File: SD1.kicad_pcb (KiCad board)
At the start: 4 copper layers, 107.8 x 108 mm, 251 parts, among them J101 JST 1.25mm, J102 JST 1.25mm, J103 JST ZH 1.5mm 1x5, J201 HR861153C, J301 PJ-102AH, J302 PJ-102AH, J303 Conn_01x02, J304 Conn_01x02, J402 FTDI_TTL_Cable, J403 10118194-0001LF, J404 Conn_ARM_JTAG_SWD_10, J801 Conn_01x02, J802 Conn_01x02, Q101 BSS138, Q102 PDTC114EU,115, Q301 DMMT5401, Q302 DMMT5401, Q303 FDT86244, Q801 DMMT5401, Q802 DMMT5401, SW101 Multidirection_Switch, SW401 PTS810, T301 HR051067, U101 ER-TFTM028-4, U102 MCP23017, U103 CC2652P, U104 SCD30, U105 BME280, U106 EKMC1691111, U201 W5500, U301 TPS23753A, U302 TL431A, U303 TCMT1107, U401 CP2102N-A02-GQFN28R, U501 CCS811, U601 110-102, U602 LMP91000, U701 TLV70018, U702 ADPD188BI, U703 Smoke Chamber, U801 TPS61022, U802 TLV62585, U803 MCP73831-2-OT, Y201 25MHz

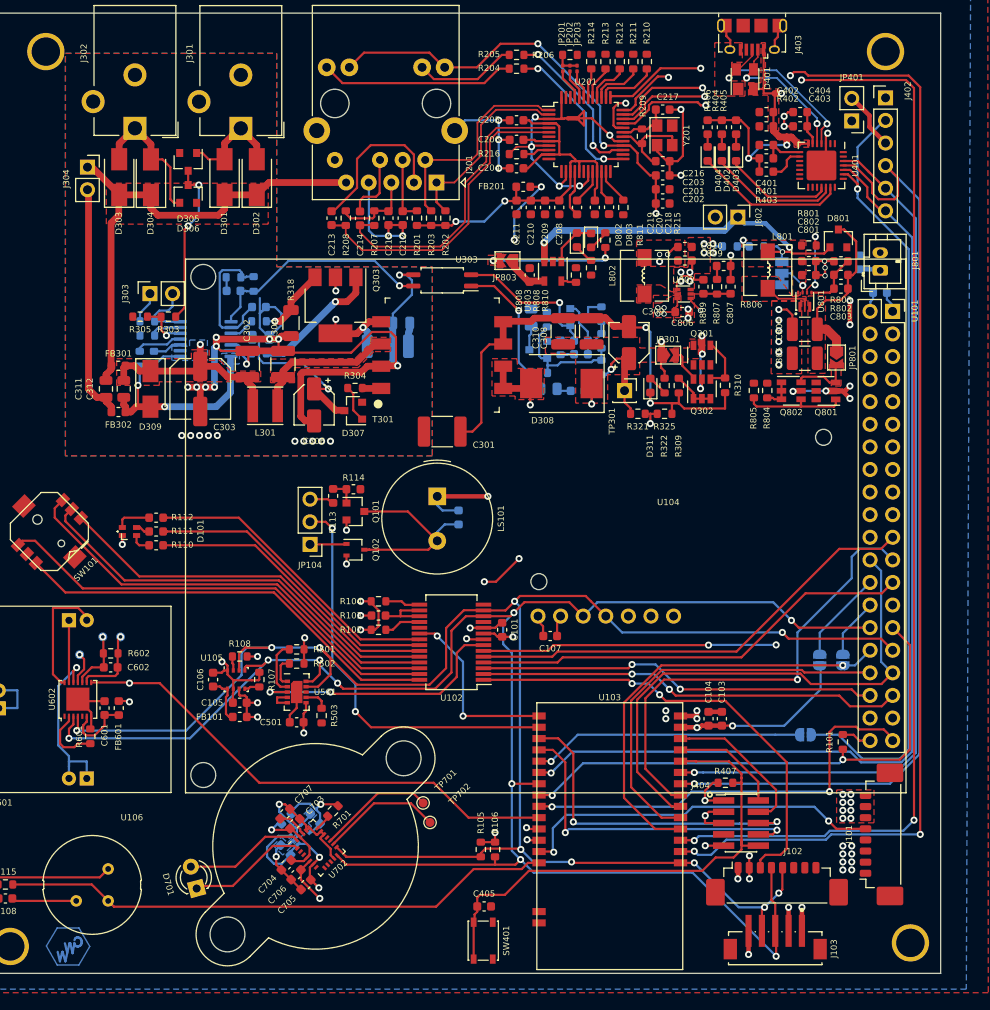
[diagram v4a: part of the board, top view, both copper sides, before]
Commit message: BOM reduction and part picking
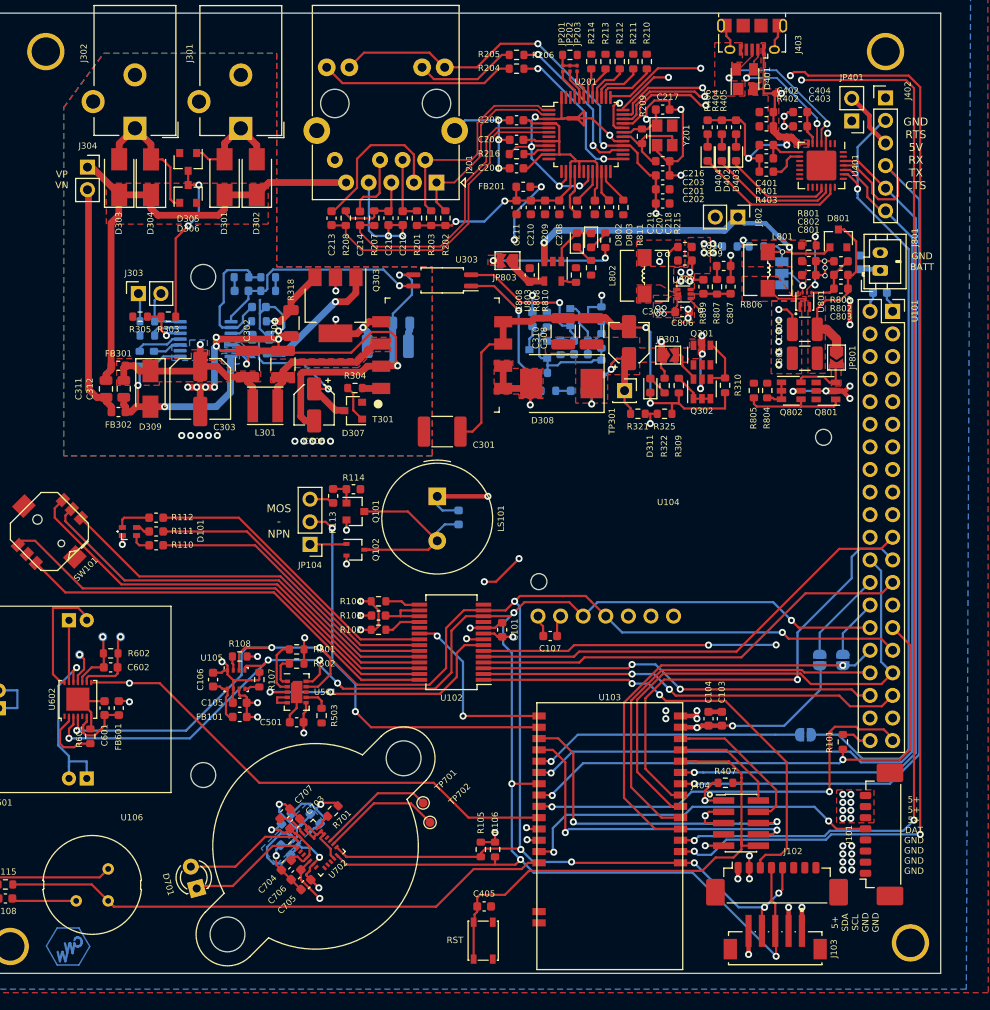
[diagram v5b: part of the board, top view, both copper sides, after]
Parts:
- added R326: 1k, Resistor_SMD:R_0603_1608Metric, B.Cu at (147.8, 36.2)
- C317: footprint Capacitor_SMD:C_0805_2012Metric -> Capacitor_SMD:C_0603_1608Metric
- Q301, Q801: value DMMT5401 -> DMP3098L-7
- R114, R601: value 499k -> 732k
- R302: value 20 -> 22.1; footprint Resistor_SMD:R_0805_2012Metric -> Resistor_SMD:R_0603_1608Metric
- R323: value 2k -> 1k
- moved R323 1.82 mm to (147.8, 37.7), turned to 180 degrees
- moved J303 1.31 mm to (133.2, 38.0)
- moved C318 0.90 mm to (144.8, 37.7)
- moved R320 0.90 mm to (144.8, 36.2)
- moved C317 0.24 mm to (177.5, 40.9)
- moved R302 0.23 mm to (179.3, 48.9)
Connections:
- R323 pad 1: Net-(C315-Pad1) -> Net-(R323-Pad1)
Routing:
- net GND: track 233.3 -> 243.8 mm, vias 57 -> 60
- net Net-(R323-Pad1): track 0.00 -> 1.51 mm
- net Net-(J303-Pad2): track 7.48 -> 6.39 mm
- net SPI_SCK: track 150.2 -> 151.2 mm
- net SPI_MISO: track 151.3 -> 152.2 mm
- net Net-(C703-Pad1): track 9.91 -> 10.7 mm
- net +3V3: track 463.4 -> 463.9 mm
- added copper zone on B.Cu, net Net-(R311-Pad2)
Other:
- board text added: "5+ 5+ 5+ DAT GND GND GND GND"
- board text added: "5+ SDA SCL GND GND"
- board text added: "DO"
- board text added: "GND BATT"
- board text added: "GND RTS 5V RX TX CTS"
- board text added: "MOS - NPN"
- board text added: "RD"
- board text added: "RST"
- board text added: "RTS"
- board text added: "SAEMS r0, 12/12/20 Clayton White Daniel Mulvaney"
- board text added: "VP VN"
- board text removed: "SAEMS r0, 12/12/20 Daniel Mulvaney Clayton White"

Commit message: Trace length matching for ETH and USB
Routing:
- net /Debug and Serial/USB_DN: track 16.4 -> 20.4 mm

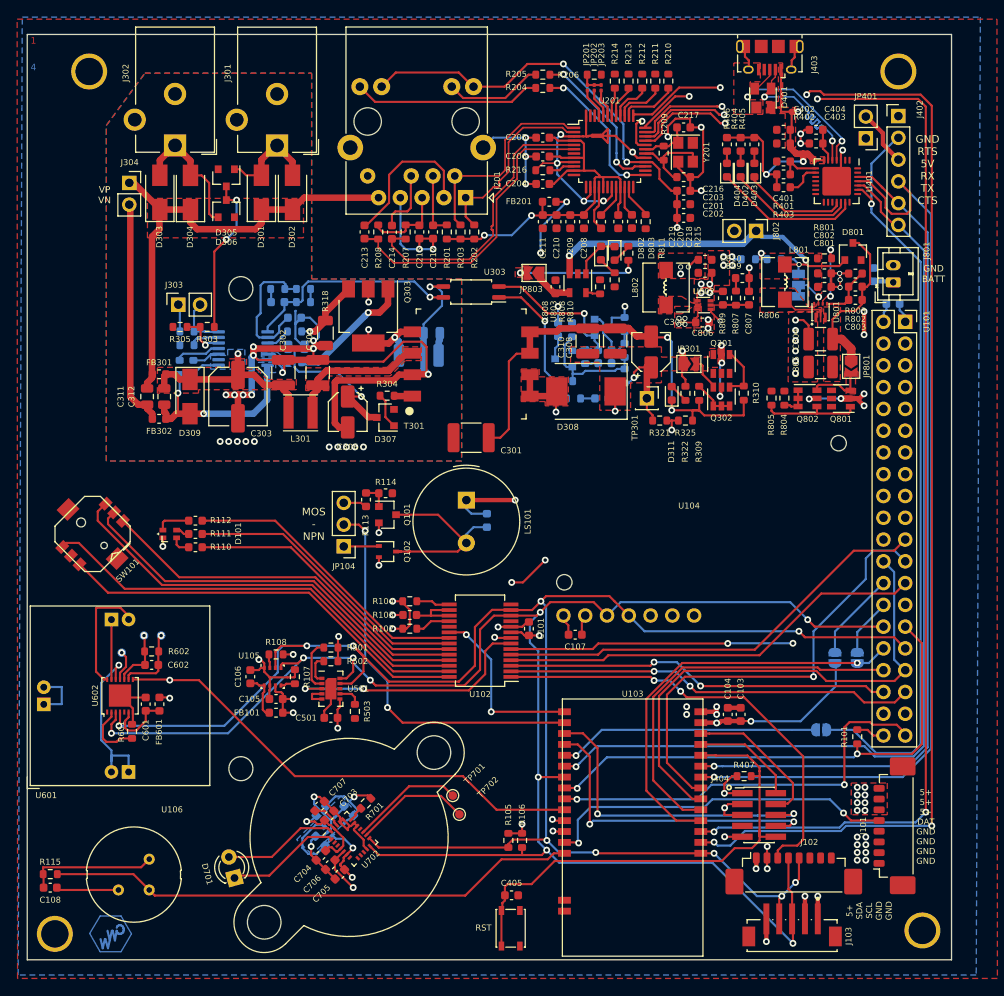
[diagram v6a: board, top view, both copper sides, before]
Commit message: Prep for gerber export
Update fields
Align standoff holes
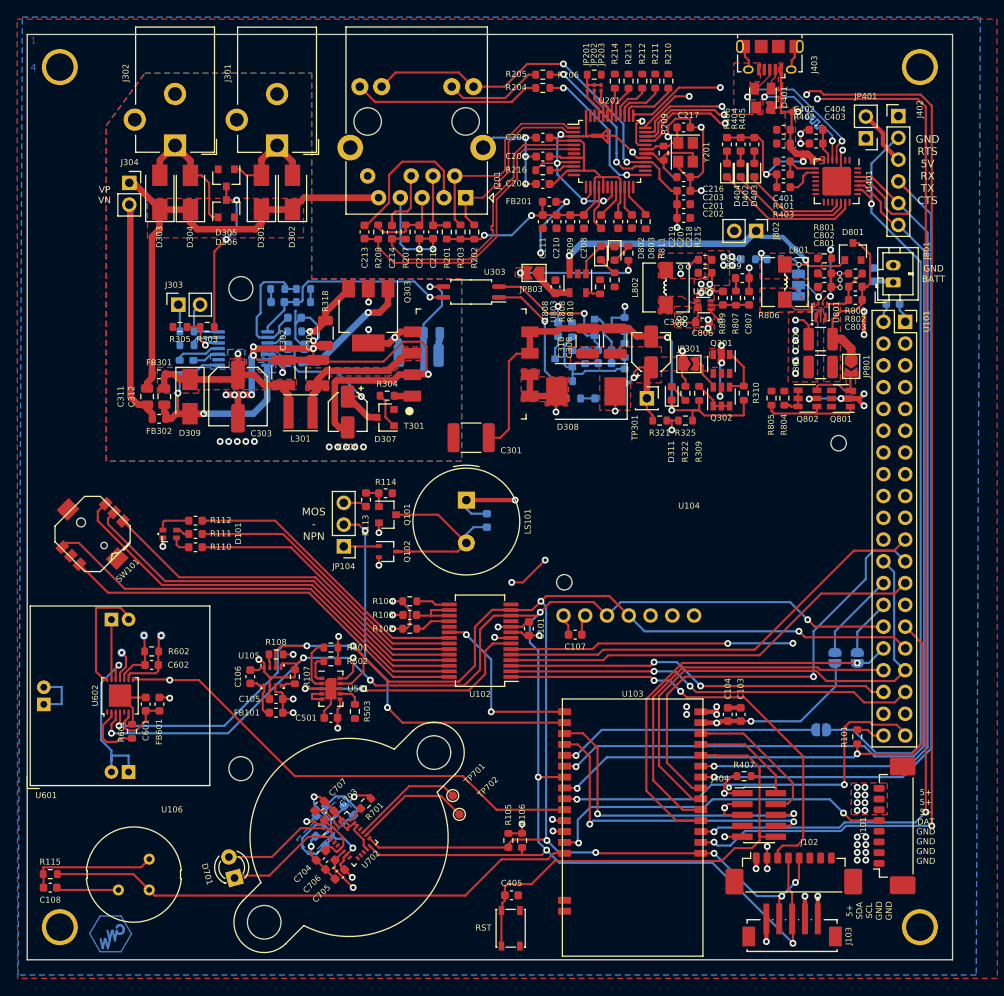
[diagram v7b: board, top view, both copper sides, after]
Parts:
- moved MK101 3.46 mm to (119.4, 10.3)
- moved MK102 2.56 mm to (219.7, 10.3)
- moved MK104 0.97 mm to (119.4, 110.6)
- moved MK103 0.48 mm to (219.7, 110.6)
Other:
- board size 107.8 x 108 mm -> 108 x 108 mm
- rule pad_to_mask_clearance: 0.05 -> 0
- board text added: "SAEMS r0, 12/14/20 Clayton White Daniel Mulvaney"
- board text removed: "SAEMS r0, 12/12/20 Clayton White Daniel Mulvaney"

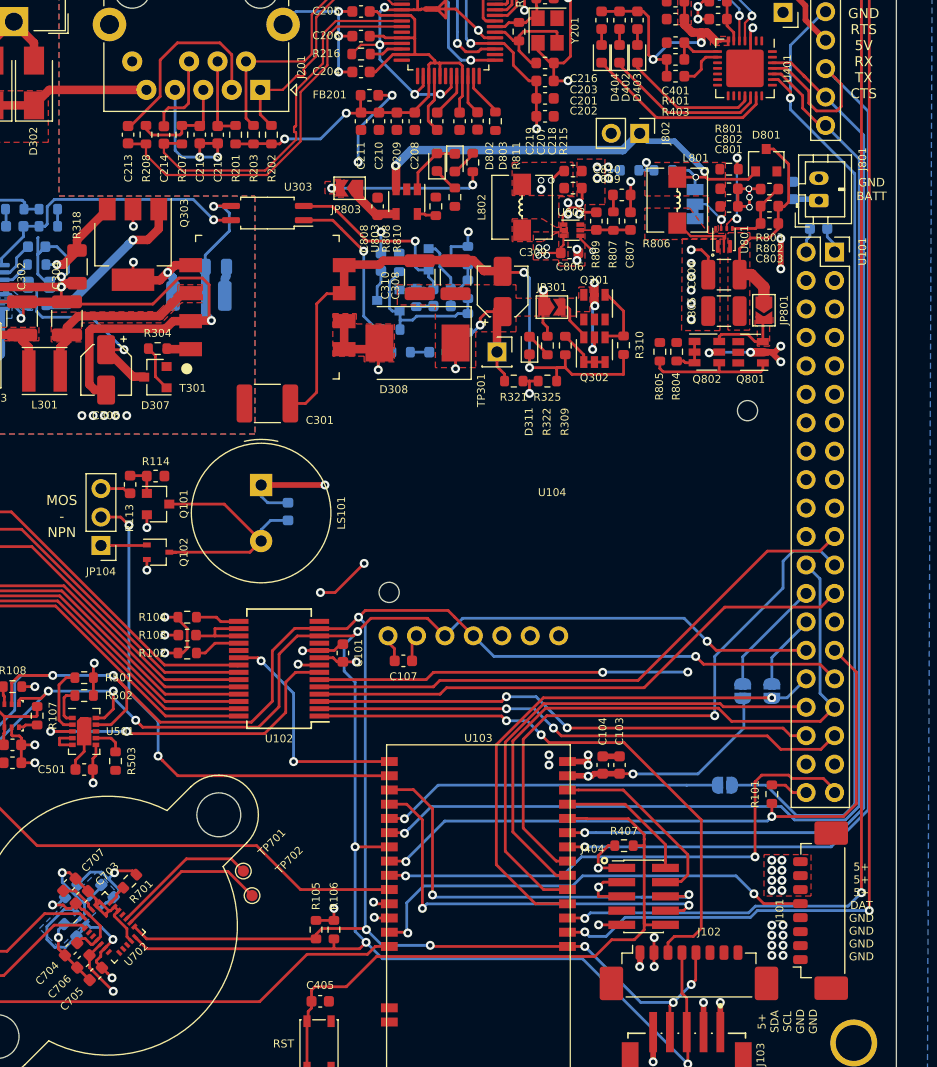
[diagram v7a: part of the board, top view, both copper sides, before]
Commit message: Increase clearance for SWD connector
Alternatives are:
FTSH-105-01-L-DV-K
BXIDM03
3221-10-0300-00
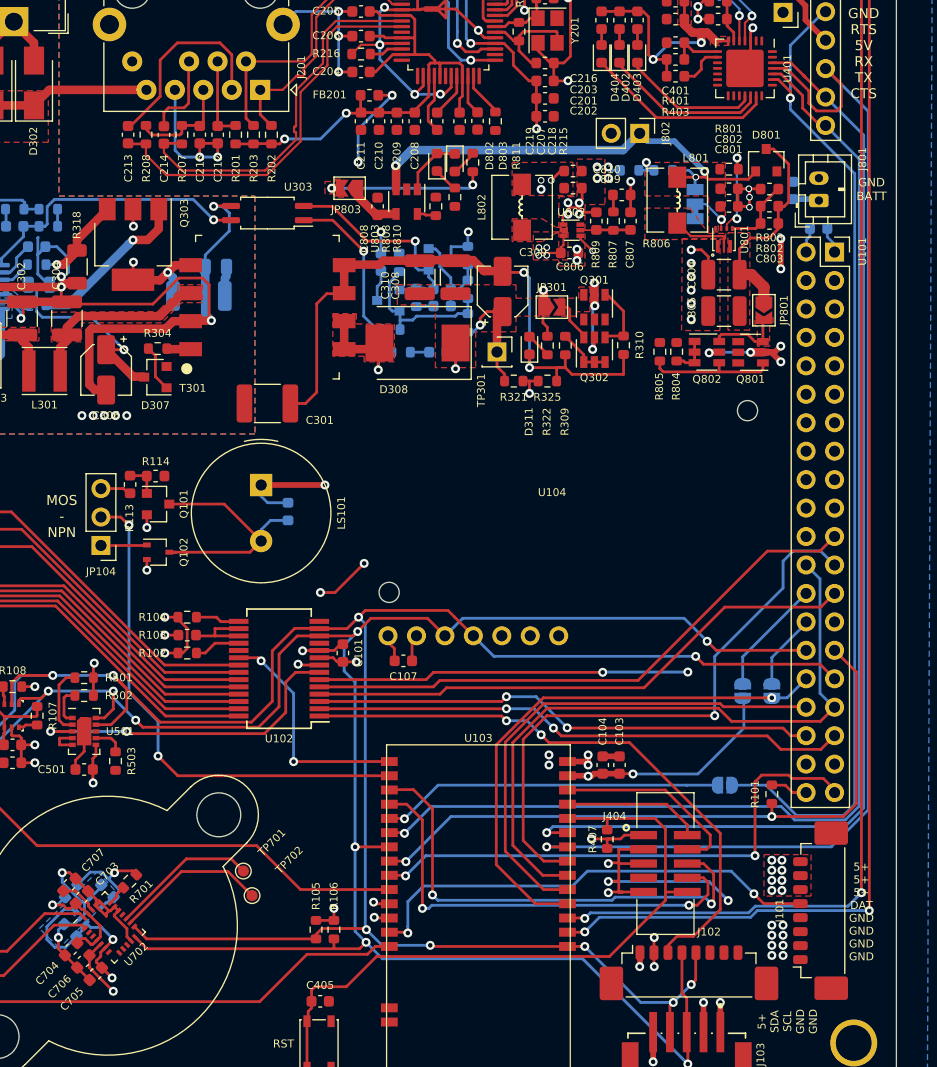
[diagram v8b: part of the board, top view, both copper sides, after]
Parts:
- J404: footprint mylib:PinHeader_2x05_P1.27mm_Thin_Shrouded_Vertical_SMD -> mylib:PinHeader_2x05_P1.27mm_Wide_Shrouded_Vertical_SMD
- moved J404 3.52 mm to (202.9, 94.6)
- moved R407 1.61 mm to (197.7, 92.4), turned to 270 degrees
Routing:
- net GND: track 243.8 -> 261.7 mm, vias 60 -> 62
- net /DIO16_TDO: track 37.8 -> 43.3 mm
- net /DIO12_RXD: track 108.5 -> 112.2 mm
- net /DIO13_TXD: track 98.5 -> 102.2 mm
- net +3V3: track 463.9 -> 461.0 mm
- net /DIO17_TDI: track 37.7 -> 40.5 mm
- net /WMCU_RESET: track 58.6 -> 60.5 mm
- net /EXT_Sleep: track 52.0 -> 53.6 mm
- net /~LCD_CS: track 52.9 -> 53.5 mm
- net SPI_SCK: track 151.2 -> 151.8 mm
